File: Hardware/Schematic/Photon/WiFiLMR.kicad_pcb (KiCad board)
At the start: 2 copper layers, 58 parts, among them J1 Conn_01x12, J10 Conn_01x02, J11 Conn_01x01, J12 Conn_01x01, J13 Conn_01x24, J14 Conn_01x01, J15 Conn_01x01, J16 Conn_01x01, J17 Conn_01x01, J18 Conn_01x01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

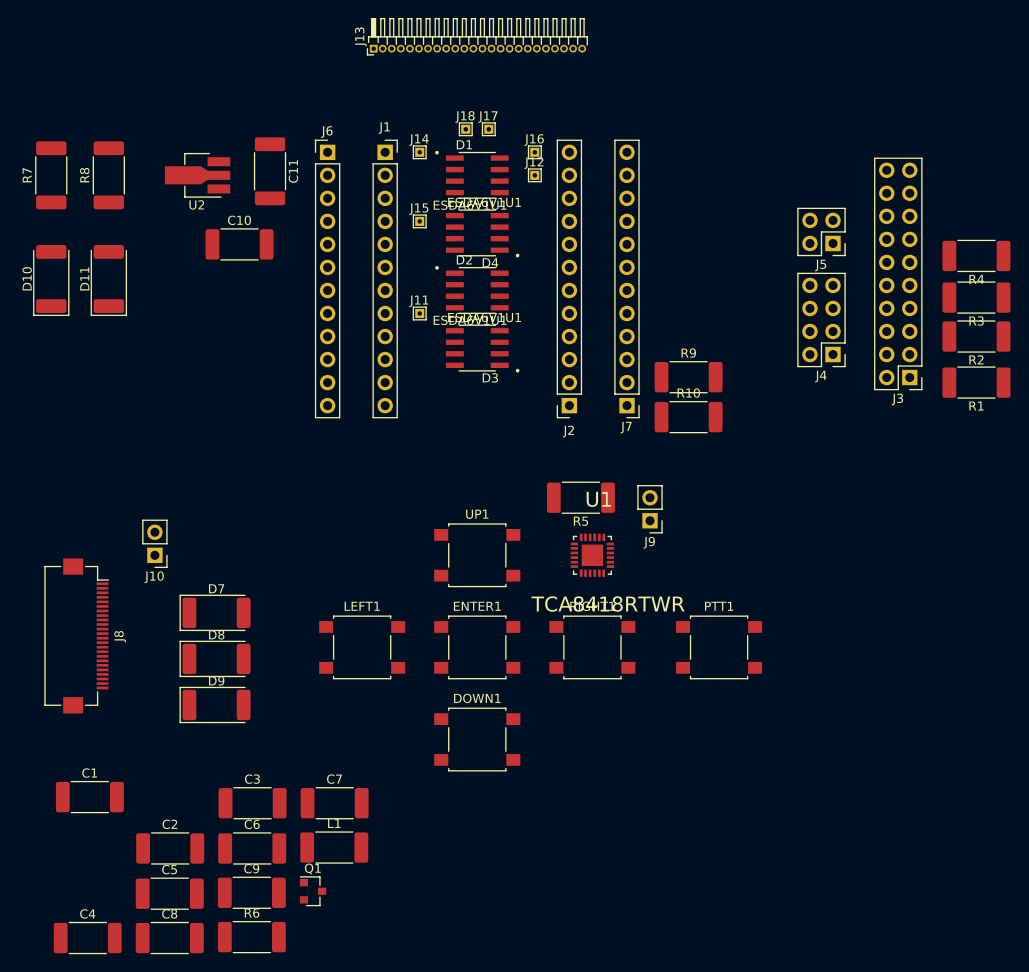
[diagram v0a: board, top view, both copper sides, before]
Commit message: Split-up schematics into three seperate projects with a parts library as well
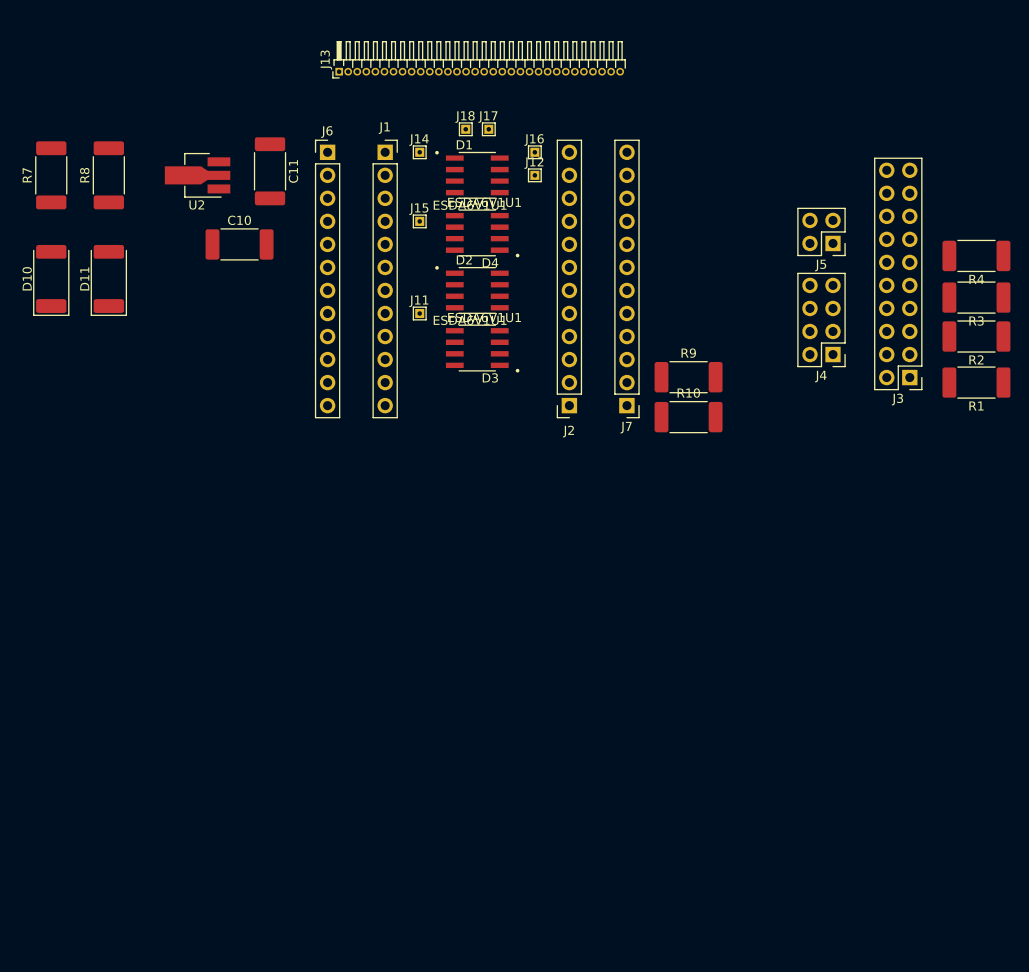
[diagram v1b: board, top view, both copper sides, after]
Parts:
- removed C1: 0.1uF, Capacitor_SMD:C_2512_6332Metric_Pad1.52x3.35mm_HandSolder
- removed C2, C4, C5, C6, C7, C8, C9: 1uF, Capacitor_SMD:C_2512_6332Metric_Pad1.52x3.35mm_HandSolder
- removed C3: 4.7uF, Capacitor_SMD:C_2512_6332Metric_Pad1.52x3.35mm_HandSolder
- removed D7, D8, D9: D_Schottky, Diode_SMD:D_2512_6332Metric_Pad1.52x3.35mm_HandSolder
- removed DOWN1, ENTER1, LEFT1, PTT1, RIGHT1, UP1: SW_Push, Button_Switch_SMD:SW_SPST_B3S-1000
- removed J10, J9: Conn_01x02, Connector_PinHeader_2.54mm:PinHeader_1x02_P2.54mm_Vertical
- removed J8: Conn_01x24, Connector_FFC-FPC:Hirose_FH12-24S-0.5SH_1x24-1MP_P0.50mm_Horizontal
- removed L1: 10uH, Inductor_SMD:L_2512_6332Metric_Pad1.52x3.35mm_HandSolder
- removed Q1: Q_PJFET_GSD, Package_TO_SOT_SMD:SOT-23
- removed R5: R_Small_US, Resistor_SMD:R_2512_6332Metric_Pad1.52x3.35mm_HandSolder
- removed R6: 470mOhms, Resistor_SMD:R_2512_6332Metric_Pad1.52x3.35mm_HandSolder
- removed U1: TCA8418RTWR, TCA8418RTWR:QFN50P400X400X80-25N
- J13: value Conn_01x24 -> Conn_01x32; footprint Connector_PinHeader_1.00mm:PinHeader_1x24_P1.00mm_Horizontal -> Connector_PinHeader_1.00mm:PinHeader_1x32_P1.00mm_Horizontal
- moved J13 4.58 mm to (123.2, 68.6)
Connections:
- J13 pad 1: Net-(J13-Pad1) -> +5V
- J13 pad 10: Net-(J13-Pad10) -> ADC12|SPI_SS
- J13 pad 11: Net-(J13-Pad11) -> ADC13
- J13 pad 12: Net-(J13-Pad12) -> ADC15
- J13 pad 13: Net-(J13-Pad13) -> SDA|TIM4_CH2
- J13 pad 14: Net-(J13-Pad14) -> SCL|CAN2_TX|TIM4_CH1
- J13 pad 15: Net-(J13-Pad15) -> SPI1_MOSI|CAN2_RX|TIM3_CH2|I2S3_SD
- J13 pad 16: Net-(J13-Pad16) -> JTAG_TRST|SPI1_MISO|TIM3_CH1
- J13 pad 17: Net-(J13-Pad17) -> JTAG_TDO|SPI1_SCK|I2S3_SCK
- J13 pad 18: Net-(J13-Pad18) -> JTAG_TDI|SPI1_SS|I2S3_WS
- J13 pad 19: Net-(J13-Pad19) -> JTAG_TCK
- J13 pad 2: Net-(J13-Pad2) -> Earth
- J13 pad 20: Net-(J13-Pad20) -> JTAG_TMS
- J13 pad 21: Net-(J13-Pad21) -> Earth
- J13 pad 22: Net-(J13-Pad22) -> +BATT
- J13 pad 23: Net-(J13-Pad23) -> RST
- J13 pad 24: Net-(J13-Pad24) -> +3V3
- J13 pad 3: Net-(J13-Pad3) -> USART1_TX|TIM1_CH2
- J13 pad 4: Net-(J13-Pad4) -> USART1_RX|TIM1_CH3
- J13 pad 5: Net-(J13-Pad5) -> WKUP|ADC0|TIM5_CH1
- J13 pad 6: Net-(J13-Pad6) -> ADC4|DAC1
- J13 pad 7: Net-(J13-Pad7) -> ADC7|SPI_MOSI|TIM3|CH2
- J13 pad 8: Net-(J13-Pad8) -> ADC6|SPI_MISO|TIM3_CH1
- J13 pad 9: Net-(J13-Pad9) -> ADC5|SPI_SCK|DAC2

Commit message: Added a barrel jack connector to the photon board
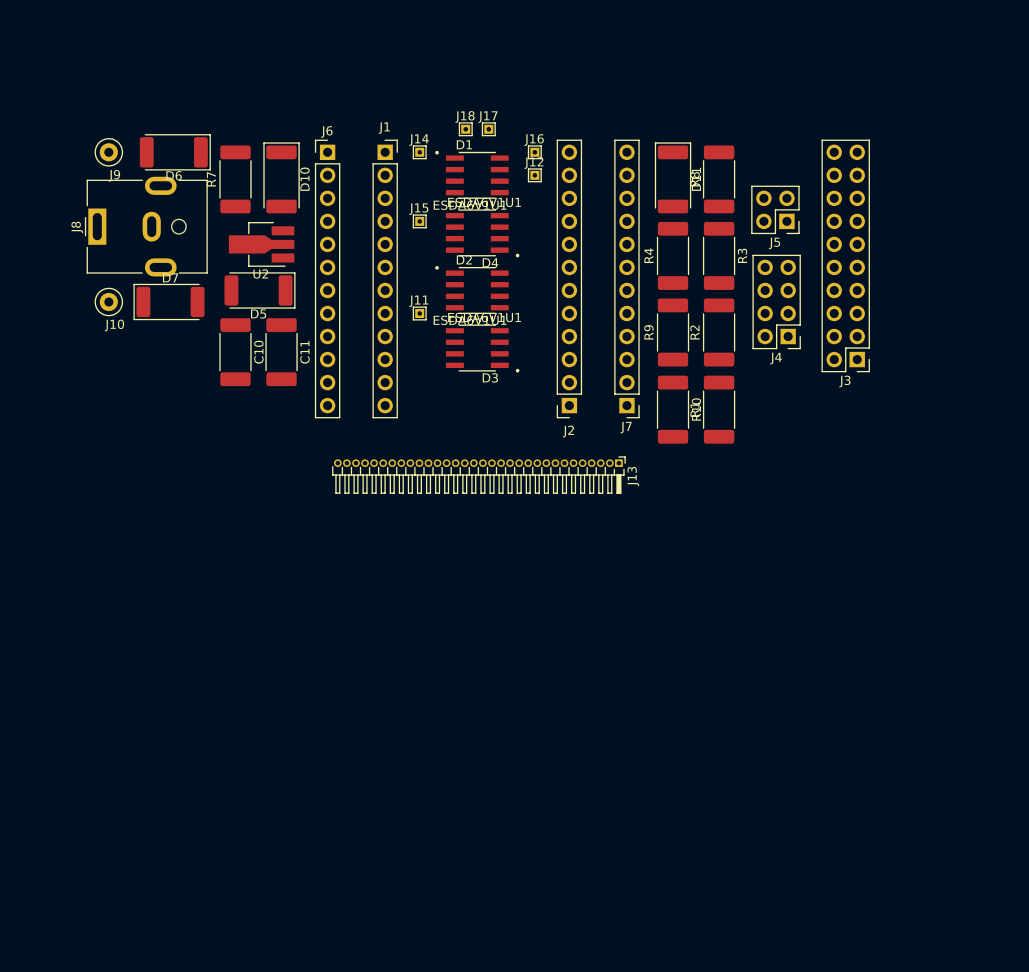
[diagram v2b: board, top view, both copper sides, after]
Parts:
- added D5: D, Diode_SMD:D_2512_6332Metric_Pad1.52x3.35mm_HandSolder, F.Cu at (114.3, 92.7)
- added D6: D, Diode_SMD:D_2512_6332Metric_Pad1.52x3.35mm_HandSolder, F.Cu at (105.0, 77.5)
- added D7: D, Diode_SMD:D_2512_6332Metric_Pad1.52x3.35mm_HandSolder, F.Cu at (104.6, 94.0)
- added J10: Conn_01x01, TestPoint:TestPoint_Loop_D2.50mm_Drill1.0mm, F.Cu at (97.8, 94.0)
- added J8: Barrel_Jack_MountingPin, Connector_BarrelJack:BarrelJack_CUI_PJ-063AH_Horizontal, F.Cu at (96.5, 85.7)
- added J9: Conn_01x01, TestPoint:TestPoint_Loop_D2.50mm_Drill1.0mm, F.Cu at (97.8, 77.5)
- moved R8 67.3 mm to (165.1, 80.5)
- moved D11 63.2 mm to (160.0, 80.5), turned to 270 degrees
- moved J13 53.1 mm to (154.1, 111.8), turned to 270 degrees
- moved R4 33.5 mm to (160.0, 88.9), turned to 90 degrees
- moved R3 28.8 mm to (165.1, 88.9), turned to 270 degrees
- moved R1 28.5 mm to (165.1, 105.9), turned to 90 degrees
- moved R2 28.4 mm to (165.1, 97.3), turned to 90 degrees
- moved D10 27.7 mm to (116.8, 80.5), turned to 270 degrees
- moved R7 20.3 mm to (111.8, 80.5)
- moved C11 20.0 mm to (116.8, 99.5)
- moved C10 11.9 mm to (111.8, 99.5), turned to 270 degrees
- moved U2 10.4 mm to (115.0, 87.6)
- moved J3 6.13 mm to (180.3, 100.3)
- moved J5 5.63 mm to (172.6, 85.1)
- moved J4 5.33 mm to (172.7, 97.8)
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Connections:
- net VCC renamed Net-(C10-Pad1)

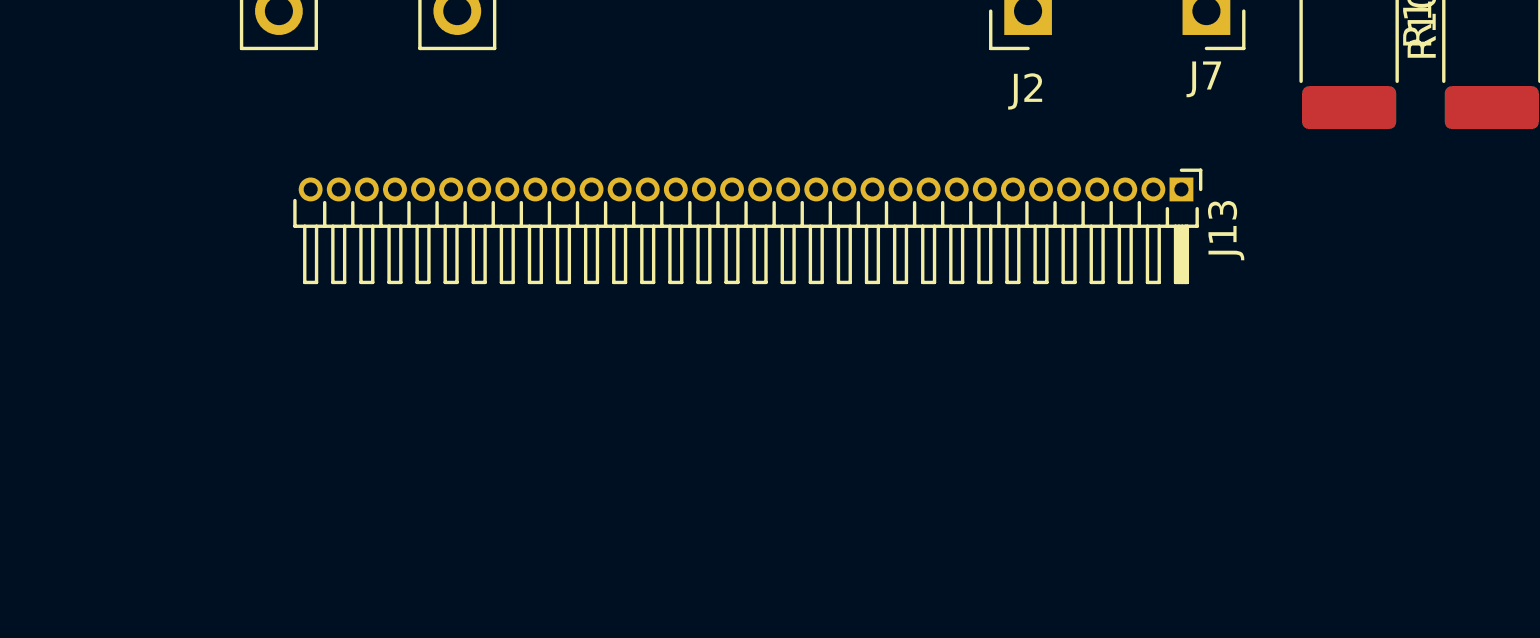
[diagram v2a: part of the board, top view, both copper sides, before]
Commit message: Updated keypad and display schematic to use header sockets for intra-board connections.
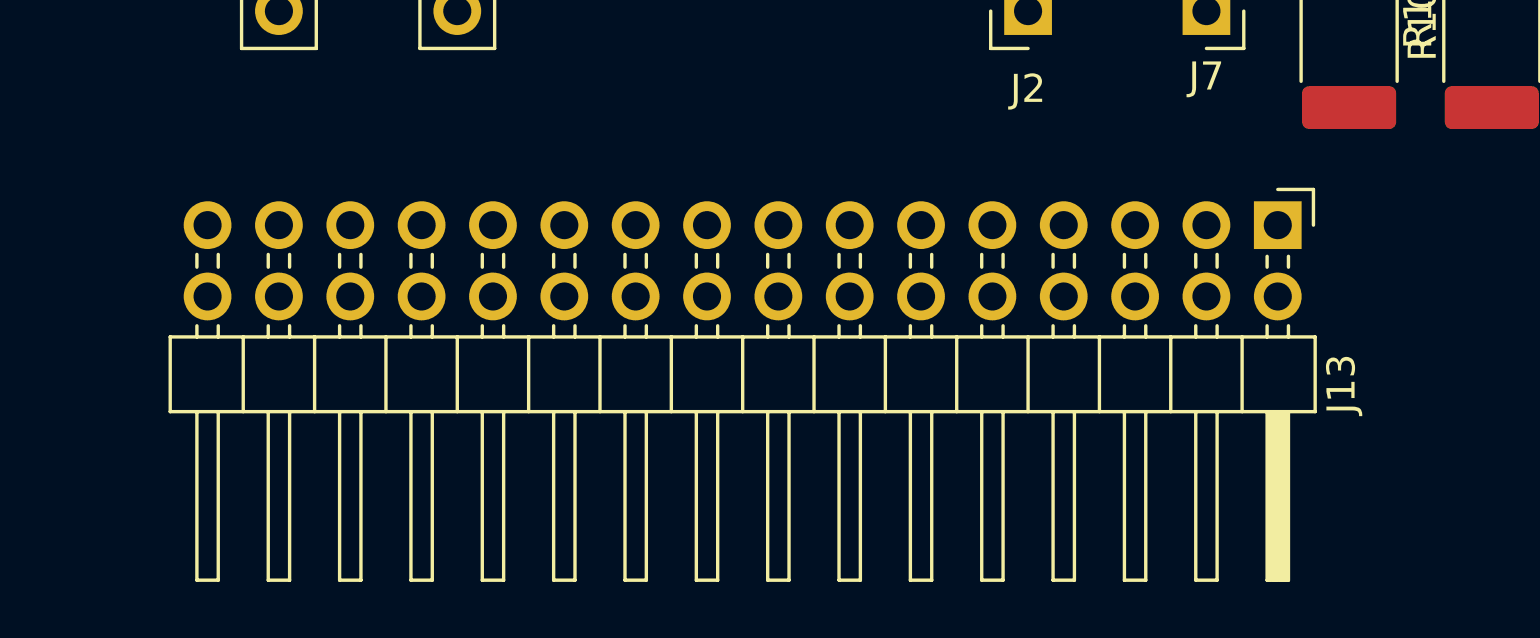
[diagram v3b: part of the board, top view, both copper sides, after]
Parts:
- J13: footprint Connector_PinHeader_1.00mm:PinHeader_1x32_P1.00mm_Horizontal -> Connector_PinHeader_2.54mm:PinHeader_2x16_P2.54mm_Horizontal
- moved J13 3.66 mm to (157.5, 113.0)
